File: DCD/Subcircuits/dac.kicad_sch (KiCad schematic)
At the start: 21 parts, among them U1 OPA277UA, U2 DAC8811ICDGKT, U2 OPA277UA, U3 OPA277UA, U4 DAC8811ICDGKT

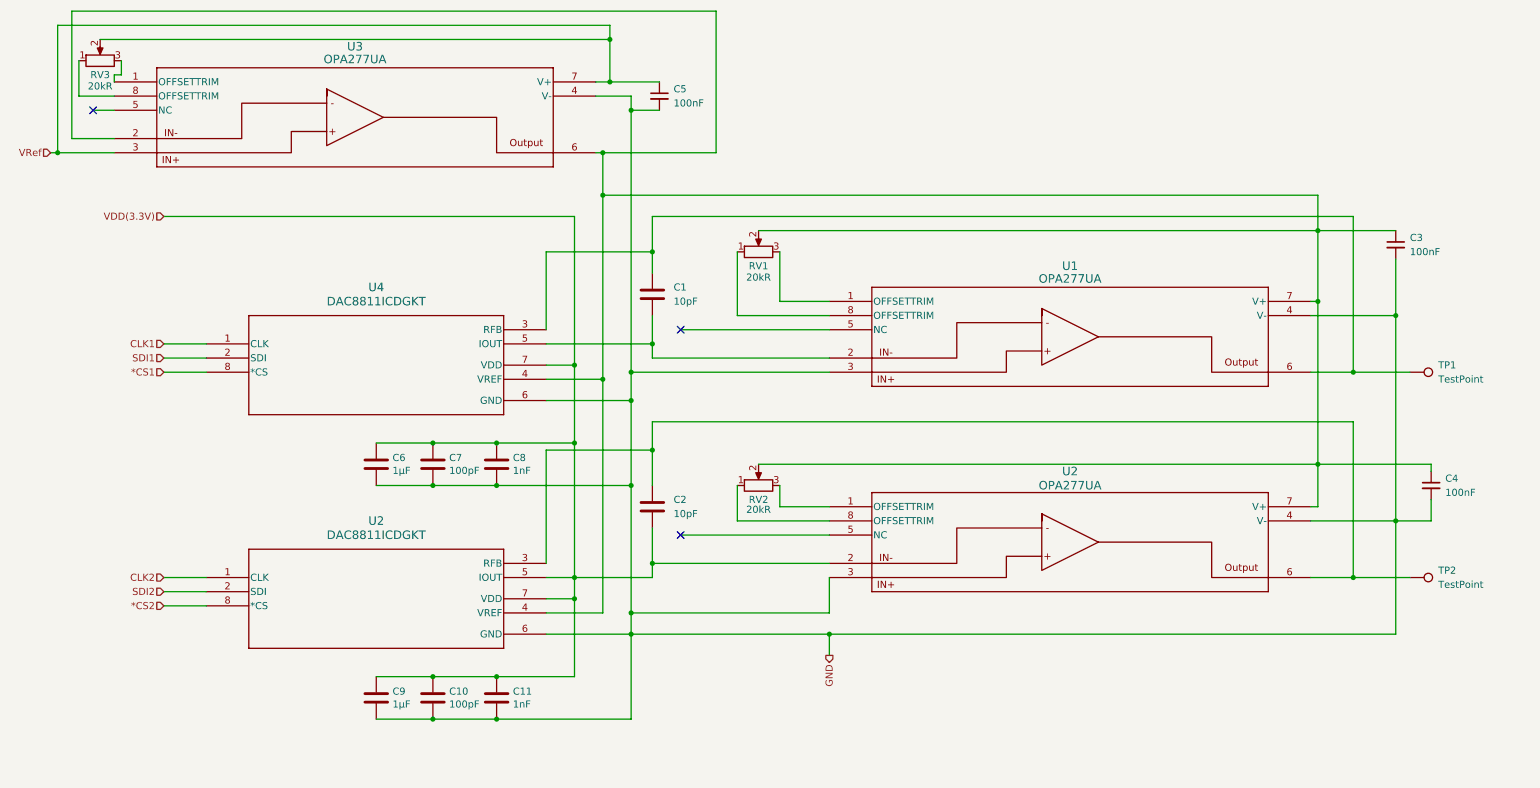
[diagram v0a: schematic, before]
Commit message: Progress on the implementation of the DAC driver
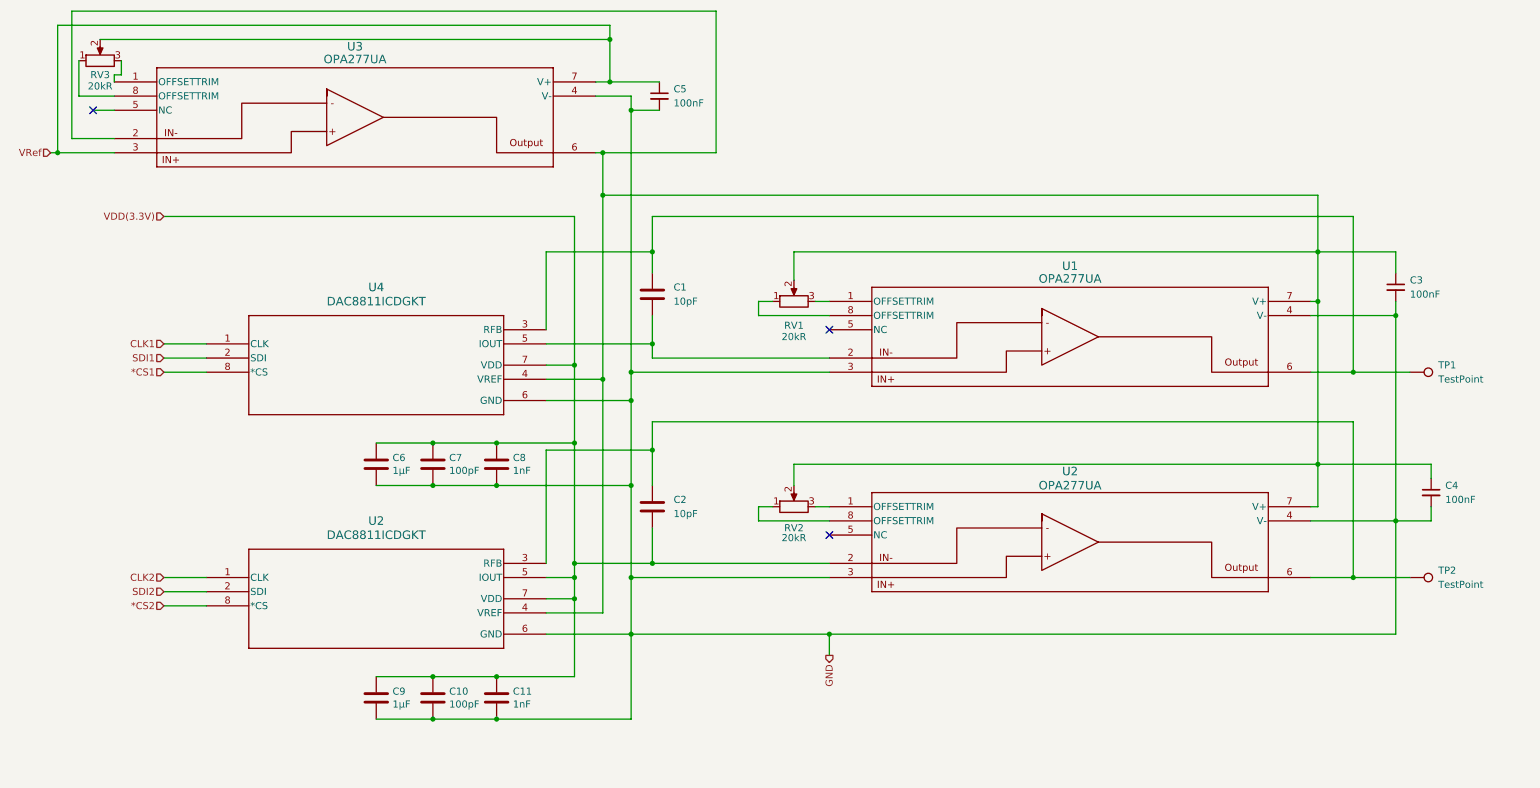
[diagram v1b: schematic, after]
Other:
- moved on the sheet: C3, C4, RV1, RV2

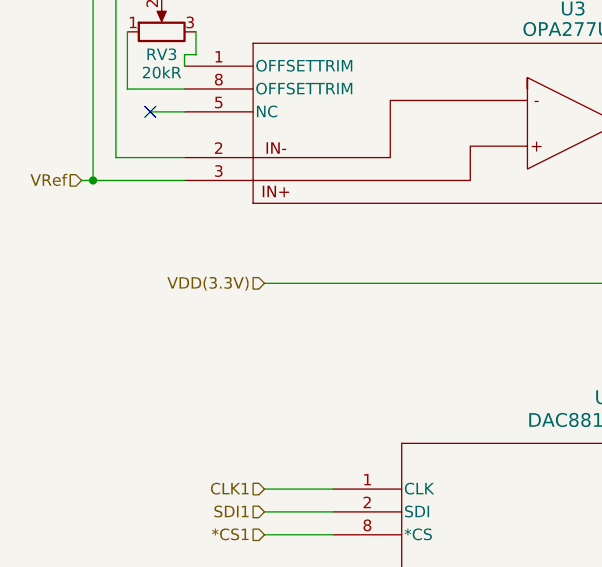
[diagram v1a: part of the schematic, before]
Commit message: Fixed the switches, finished the adc amplifier, missing the filer to adc
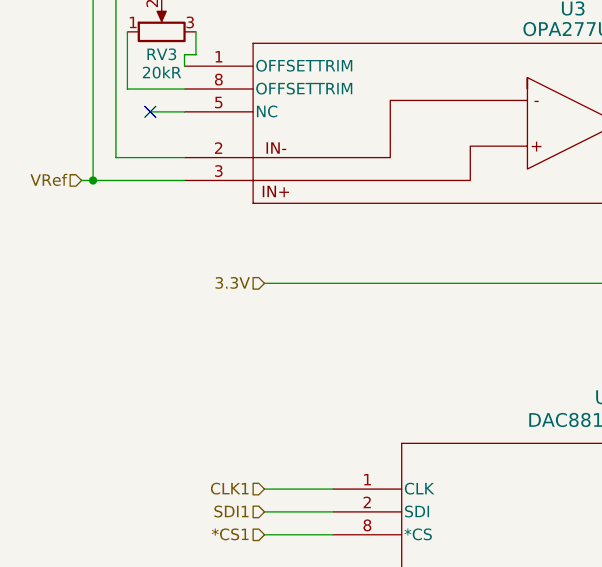
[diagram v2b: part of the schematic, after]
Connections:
- net VDD(3.3V) renamed 3.3V
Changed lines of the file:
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@@
 		)
 	)
-	(hierarchical_label "VDD(3.3V)"
+	(hierarchical_label "3.3V"
 		(shape input)
 		(at 41.91 63.5 180)
@@
 			)
 		)
-		(property "Datasheet" "${KIPRJMOD}/Datasheets/GCJ188R71H104KA12_02B-3140350.pdf"
+		(property "Datasheet" "~"
 			(at 269.24 113.03 0)
 			(effects
@@
 			)
 		)
-		(property "Description" ""
+		(property "Description" "Unpolarized capacitor, small symbol"
 			(at 269.24 113.03 0)
 			(effects
@@
 			)
 		)
-		(property "Datasheet" "${KIPRJMOD}/Datasheets/GCJ188R71H104KA12_02B-3140350.pdf"
+		(property "Datasheet" "~"
 			(at 262.89 76.2 0)
 			(effects
@@
 			)
 		)
-		(property "Description" ""
+		(property "Description" "Unpolarized capacitor, small symbol"
 			(at 262.89 76.2 0)
 			(effects
@@
 			)
 		)
-		(property "Description" ""
+		(property "Description" "Unpolarized capacitor"
 			(at 101.6 107.95 0)
 			(effects
@@
 	)
 	(symbol
-		(lib_name "DAC8811ICDGKT_1")
 		(lib_id "custom_components:DAC8811ICDGKT")
 		(at 49.53 128.27 0)
@@
 			)
 		)
-		(property "Description" ""
+		(property "Description" "Unpolarized capacitor"
 			(at 90.17 149.86 0)
 			(effects
@@
 			)
 		)
-		(property "Description" ""
+		(property "Description" "Unpolarized capacitor"
 			(at 80.01 107.95 0)
 			(effects
@@
 			)
 		)
-		(property "Datasheet" "${KIPRJMOD}/Datasheets/GCJ188R71H104KA12_02B-3140350.pdf"
+		(property "Datasheet" "~"
 			(at 130.81 41.91 0)
 			(effects
@@
 			)
 		)
-		(property "Description" ""
+		(property "Description" "Unpolarized capacitor, small symbol"
 			(at 130.81 41.91 0)
 			(effects
@@
 	)
 	(symbol
-		(lib_name "DAC8811ICDGKT_1")
 		(lib_id "custom_components:DAC8811ICDGKT")
 		(at 49.53 86.36 0)
@@
 			)
 		)
-		(property "Description" ""
+		(property "Description" "Unpolarized capacitor"
 			(at 101.6 149.86 0)
 			(effects
@@
 			)
 		)
-		(property "Description" ""
+		(property "Description" "Unpolarized capacitor"
 			(at 80.01 149.86 0)
 			(effects
@@
 			)
 		)
-		(property "Description" ""
+		(property "Description" "Unpolarized capacitor"
 			(at 90.17 107.95 0)
 			(effects

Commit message: Finished the schematics. Fixed the comments that we recieved
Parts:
- removed C10, C7: 100pF, Capacitor_SMD:C_0603_1608Metric, symbol Device:C
- removed C11, C8: 1nF, Capacitor_SMD:C_0603_1608Metric, symbol Device:C
- added C33, C34: 100p, Capacitor_SMD:C_0603_1608Metric, symbol Device:C_Small
- added C35, C36: 1nF, Capacitor_SMD:C_0603_1608Metric, symbol Device:C
- renumbered C6 to C31, C9 to C32, C1 to C37, C2 to C38, C5 to C39, C3 to C40, C4 to C41, RV3 to RV1, RV1 to RV2, RV2 to RV3, U2 to U10, U1 to U11, U2 to U12, U3 to U8, U4 to U9
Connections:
- net 3.3V: now also C33.1, C34.1, C35.1, C36.1; no longer C38.2, U10.5 (IOUT), U12.2
- net GND: now also C33.2, C34.2, C35.2, C36.2
- net VRef_Ext: now reaches C40.1, C41.1, RV2.2, RV3.2, U10.4 (VREF), U11.7 (V+), U12.7 (V+), U8.2, U8.6, U9.4 (VREF)
- net DAC0: now reaches C37.1, TP1.1, U11.6, U9.3 (RFB)
- net DAC1: now reaches C38.1, TP2.1, U10.3 (RFB), U12.6
- new net: C38.2, U10.5 (IOUT), U12.2
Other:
- moved on the sheet: TP1, TP2

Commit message: added voltage divider to dac circuits for opamps
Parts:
- added R1, R2, R3, R4: 1k, Resistor_SMD:R_0603_1608Metric, symbol Device:R
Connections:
- net GND: now also R2.2, R4.2; no longer U11.3, U12.3
- net VRef_Ext: now also R1.2, R3.2
- new net: R3.1, R4.1, U12.3
- new net: R1.1, R2.1, U11.3

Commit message: reverted last changes made to dac
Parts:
- removed R1, R2, R3, R4: 1k, Resistor_SMD:R_0603_1608Metric, symbol Device:R
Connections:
- net GND: now also U11.3, U12.3

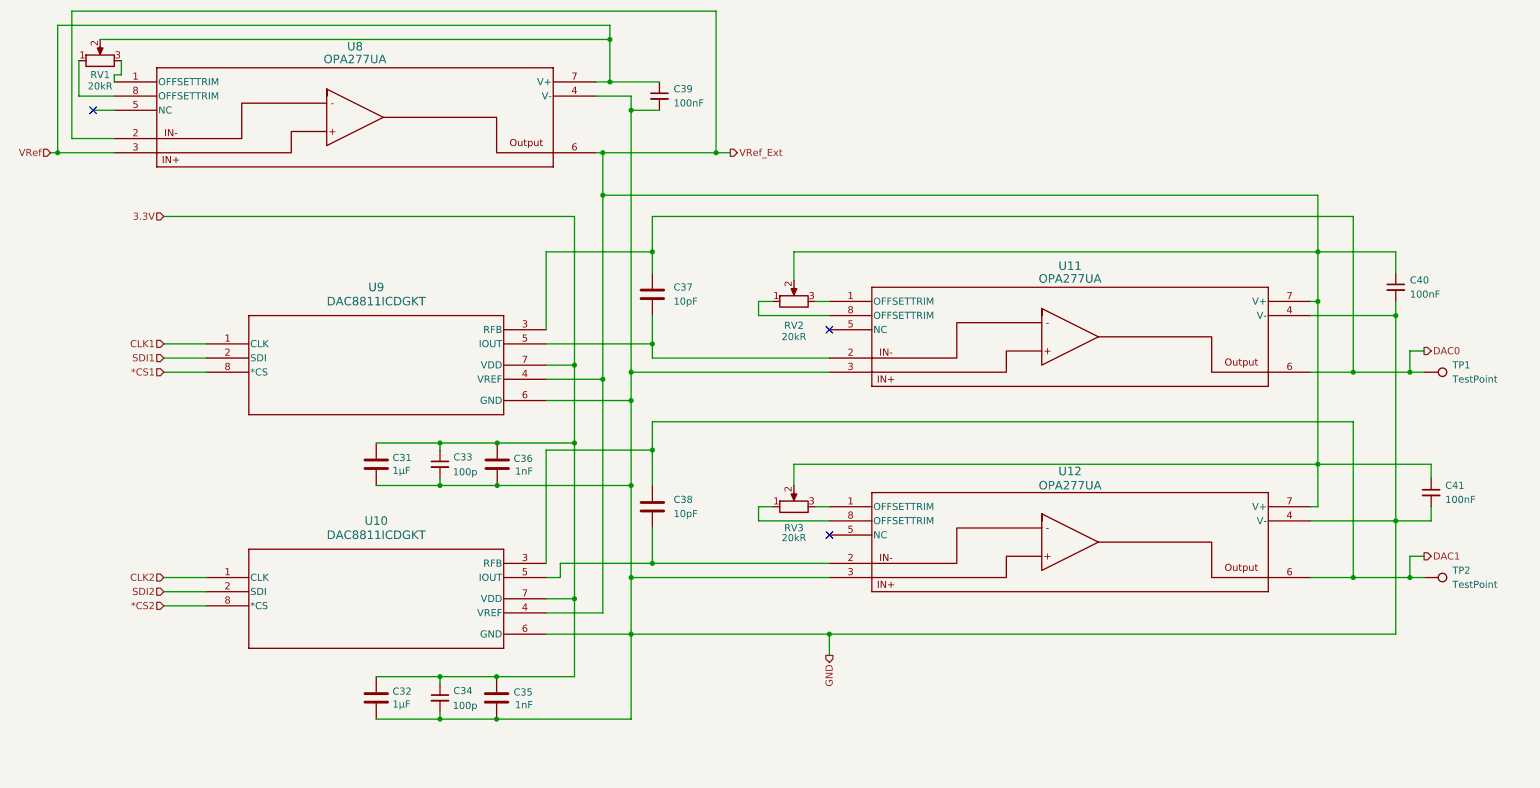
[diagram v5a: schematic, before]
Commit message: 7v and -1.2V supplying opa277s
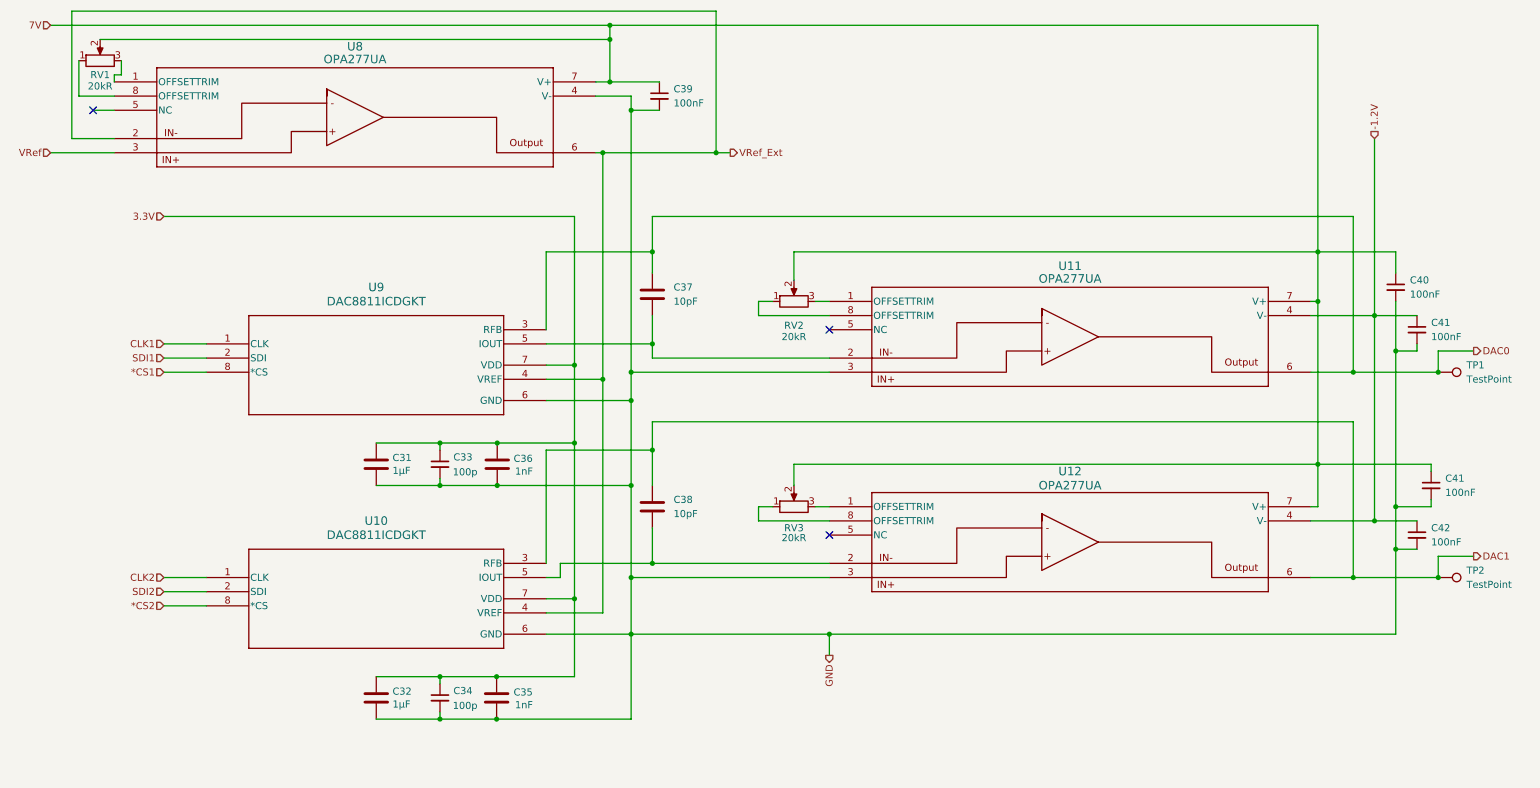
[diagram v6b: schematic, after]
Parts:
- added C41, C42: 100nF, Capacitor_SMD:C_0603_1608Metric, symbol Device:C_Small
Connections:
- net GND: now also C41.2, C42.2; no longer U11.4 (V-), U12.4 (V-)
- net VRef: no longer C39.1, RV1.2, U8.7 (V+)
- net VRef_Ext: no longer C40.1, C41.1, RV2.2, RV3.2, U11.7 (V+), U12.7 (V+)
- new net -1.2V: C41.1, C42.1, U11.4 (V-), U12.4 (V-)
- new net 7V: C39.1, C40.1, C41.1, RV1.2, RV2.2, RV3.2, U11.7 (V+), U12.7 (V+), U8.7 (V+)
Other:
- moved on the sheet: C41, TP1, TP2
